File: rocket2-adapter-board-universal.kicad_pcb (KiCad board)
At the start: 2 copper layers, 45 x 55 mm, 15 parts, among them J2 Conn_01x04_Socket, J3 Conn_01x02_Socket, J4 Conn_01x04_Socket, J5 DSUB_15pin/VGA Veritical Fema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

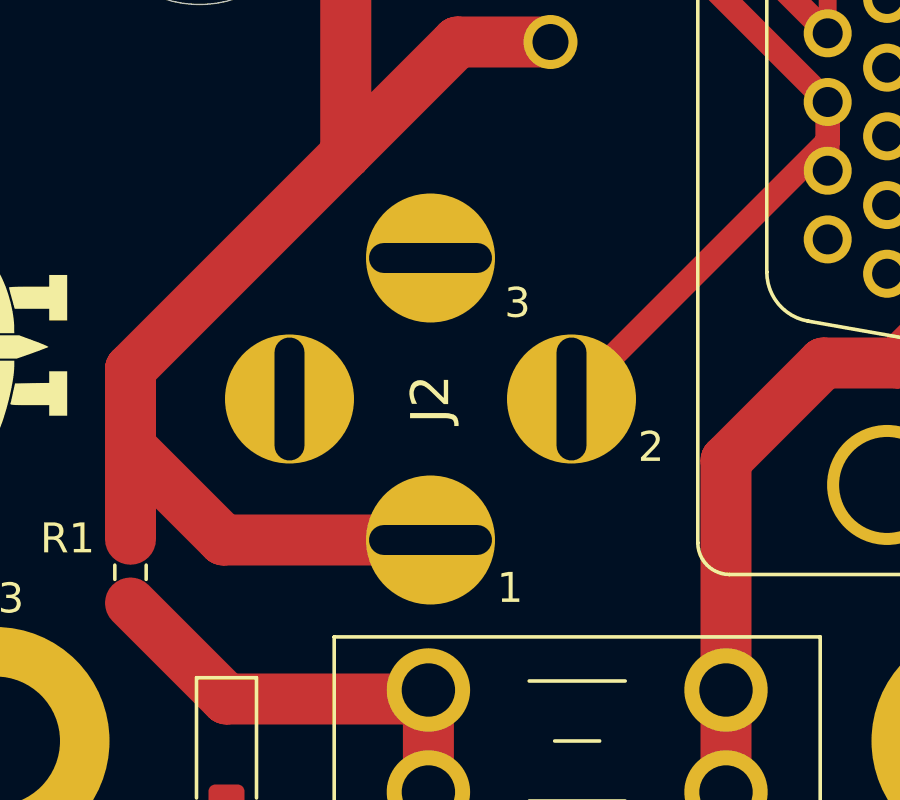
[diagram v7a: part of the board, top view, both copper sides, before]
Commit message: Final PT Footprint Update
Added an extra 1mm to all tolerances
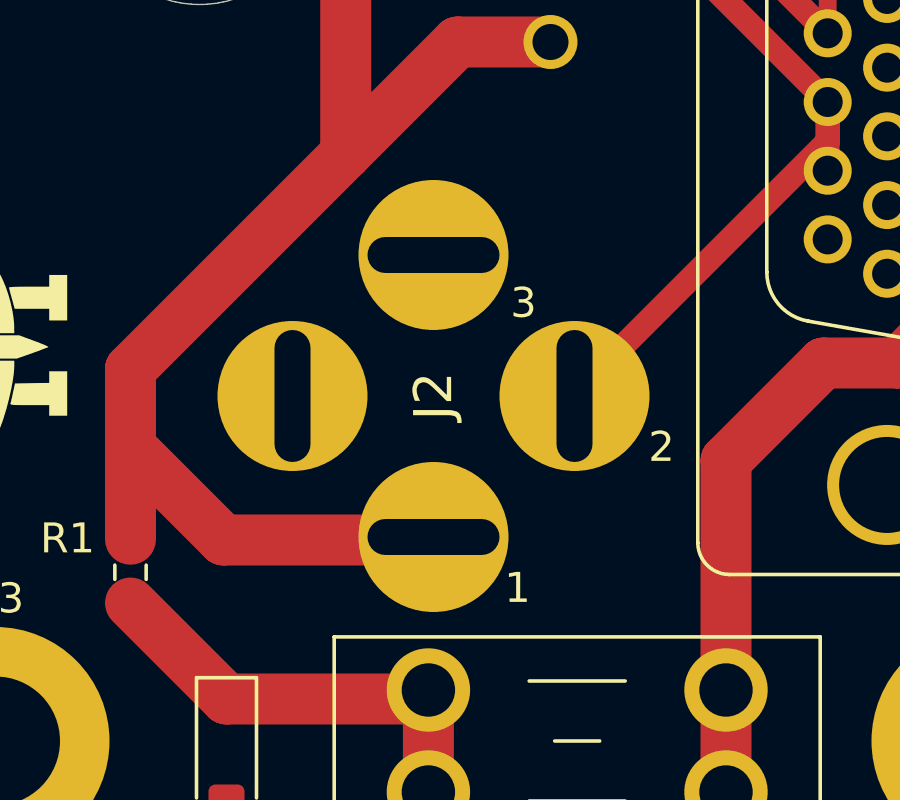
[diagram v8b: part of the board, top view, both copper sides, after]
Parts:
- moved J2 0.14 mm to (140.6, 97.5)
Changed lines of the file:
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@@
 	(net 9 "unconnected-(J5-Pad11)")
 	(net 10 "unconnected-(J5-Pad0)_1")
-	(footprint "UCIRP-KiCAD-Lib:Pad_Socket 9.4mm_MiniDIN"
-		(layer "F.Cu")
-		(at 140.5 97.6 90)
-		(descr "5749230-1-1")
-		(tags "Connector")
-		(property "Reference" "J2"
-			(at 0 0 90)
-			(layer "F.SilkS")
-			(effects
-				(font
-					(size 1.27 1.27)
-					(thickness 0.254)
-				)
-			)
-		)
-		(property "Value" "Conn_01x04_Socket"
-			(at -3.35 2.095 90)
-			(layer "F.SilkS")
-			(hide yes)
-			(effects
-				(font
-					(size 1.27 1.27)
-					(thickness 0.254)
-				)
-			)
-		)
-		(property "Datasheet" "~"
-			(at 0 0 90)
-			(layer "F.Fab")
-			(hide yes)
-			(effects
-				(font
-					(size 1.27 1.27)
-					(thickness 0.15)
-				)
-			)
-		)
-		(property "Description" "Generic connector, single row, 01x04, script generated"
-			(at 0 0 90)
-			(layer "F.Fab")
-			(hide yes)
-			(effects
-				(font
-					(size 1.27 1.27)
-					(thickness 0.15)
-				)
-			)
-		)
-		(property ki_fp_filters "Connector*:*_1x??_*")
-		(sheetname "/")
-		(sheetfile "rocket2-adapter-board-universal.kicad_sch")
-		(attr through_hole)
-		(fp_text user "${REFERENCE}"
-			(at -0.1 0.2 90)
-			(layer "F.Fab")
-			(effects
-				(font
-					(size 1.27 1.27)
-					(thickness 0.254)
-				)
-			)
-		)
-		(pad "1" thru_hole circle
-			(at -4.7 0 90)
-			(size 4.3 4.3)
-			(drill oval 1 4.1)
-			(layers "*.Cu" "*.Mask")
-			(remove_unused_layers no)
-			(net 5 "VBUS")
-			(pinfunction "Pin_1")
-			(pintype "passive")
-		)
-		(pad "2" thru_hole circle
-			(at 0 4.7 90)
-			(size 4.3 4.3)
-			(drill oval 4.1 1)
-			(layers "*.Cu" "*.Mask")
-			(remove_unused_layers no)
-			(net 3 "AIN+")
-			(pinfunction "Pin_2")
-			(pintype "passive")
-		)
-		(pad "3" thru_hole circle
-			(at 4.7 0 90)
-			(size 4.3 4.3)
-			(drill oval 1 4.1)
-			(layers "*.Cu" "*.Mask")
-			(remove_unused_layers no)
-			(net 2 "GND")
-			(pinfunction "Pin_3")
-			(pintype "passive")
-		)
-		(pad "4" thru_hole circle
-			(at 0 -4.7 90)
-			(size 4.3 4.3)
-			(drill oval 4.1 1)
-			(layers "*.Cu" "*.Mask")
-			(remove_unused_layers no)
-			(net 7 "unconnected-(J2-Pin_4-Pad4)")
-			(pinfunction "Pin_4")
-			(pintype "passive+no_connect")
-		)
-		(embedded_fonts no)
-		(model "5749230-1.stp"
-			(offset
-				(xyz -3.349999854 -8.510000101 6.689999957)
-			)
-			(scale
-				(xyz 1 1 1)
-			)
-			(rotate
-				(xyz -90 0 0)
-			)
-		)
-	)
 	(footprint "UCIRP-KiCAD-Lib:Connector_VGA_Vertical"
 		(layer "F.Cu")
@@
 		)
 	)
+	(footprint "UCIRP-KiCAD-Lib:Pad_Socket 9.4mm_MiniDIN"
+		(layer "F.Cu")
+		(at 140.6 97.5 90)
+		(descr "5749230-1-1")
+		(tags "Connector")
+		(property "Reference" "J2"
+			(at 0 0 90)
+			(layer "F.SilkS")
+			(effects
+				(font
+					(size 1.27 1.27)
+					(thickness 0.254)
+				)
+			)
+		)
+		(property "Value" "Conn_01x04_Socket"
+			(at -3.35 2.095 90)
+			(layer "F.SilkS")
+			(hide yes)
+			(effects
+				(font
+					(size 1.27 1.27)
+					(thickness 0.254)
+				)
+			)
+		)
+		(property "Datasheet" "~"
+			(at 0 0 90)
+			(layer "F.Fab")
+			(hide yes)
+			(effects
+				(font
+					(size 1.27 1.27)
+					(thickness 0.15)
+				)
+			)
+		)
+		(property "Description" "Generic connector, single row, 01x04, script generated"
+			(at 0 0 90)
+			(layer "F.Fab")
+			(hide yes)
+			(effects
+				(font
+					(size 1.27 1.27)
+					(thickness 0.15)
+				)
+			)
+		)
+		(property ki_fp_filters "Connector*:*_1x??_*")
+		(sheetname "/")
+		(sheetfile "rocket2-adapter-board-universal.kicad_sch")
+		(attr through_hole)
+		(fp_text user "${REFERENCE}"
+			(at -0.1 0.2 90)
+			(layer "F.Fab")
+			(effects
+				(font
+					(size 1.27 1.27)
+					(thickness 0.254)
+				)
+			)
+		)
+		(pad "1" thru_hole circle
+			(at -4.7 0 90)
+			(size 5 5)
+			(drill oval 1.2 4.4)
+			(layers "*.Cu" "*.Mask")
+			(remove_unused_layers no)
+			(net 5 "VBUS")
+			(pinfunction "Pin_1")
+			(pintype "passive")
+		)
+		(pad "2" thru_hole circle
+			(at 0 4.7 90)
+			(size 5 5)
+			(drill oval 4.4 1.2)
+			(layers "*.Cu" "*.Mask")
+			(remove_unused_layers no)
+			(net 3 "AIN+")
+			(pinfunction "Pin_2")
+			(pintype "passive")
+		)
+		(pad "3" thru_hole circle
+			(at 4.7 0 90)
+			(size 5 5)
+			(drill oval 1.2 4.4)
+			(layers "*.Cu" "*.Mask")
+			(remove_unused_layers no)
+			(net 2 "GND")
+			(pinfunction "Pin_3")
+			(pintype "passive")
+		)
+		(pad "4" thru_hole circle
+			(at 0 -4.7 90)
+			(size 5 5)
+			(drill oval 4.4 1.2)
+			(layers "*.Cu" "*.Mask")
+			(remove_unused_layers no)
+			(net 7 "unconnected-(J2-Pin_4-Pad4)")
+			(pinfunction "Pin_4")
+			(pintype "passive+no_connect")
+		)
+		(embedded_fonts no)
+		(model "5749230-1.stp"
+			(offset
+				(xyz -3.349999854 -8.510000101 6.689999957)
+			)
+			(scale
+				(xyz 1 1 1)
+			)
+			(rotate
+				(xyz -90 0 0)
+			)
+		)
+	)
 	(footprint "MountingHole:MountingHole_4.3mm_M4_ISO7380_Pad"
 		(layer "F.Cu")
@@
 	)
 	(gr_text "1\n"
-		(at 143.15 103.9 0)
+		(at 143.4 103.9 0)
 		(layer "F.SilkS")
 		(effects
@@
 	)
 	(gr_text "2"
-		(at 147.85 99.2 0)
+		(at 148.2 99.2 0)
 		(layer "F.SilkS")
 		(effects
@@
 	)
 	(gr_text "3"
-		(at 143.4 94.4 0)
+		(at 143.6 94.4 0)
 		(layer "F.SilkS")
 		(effects
